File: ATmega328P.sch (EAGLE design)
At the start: 6 parts, among them IC1 MEGA8-P, Q1 16MHz

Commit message: Controller board layout and schematic
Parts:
- added JP1: (no value), pinhead:PINHD-1X3/90
- added JP2, JP3: (no value), pinhead:PINHD-1X5/90
- added JP4: (no value), pinhead:PINHD-1X8/90
- added JP5: (no value), pinhead:PINHD-1X4/90
- added JP6: (no value), pinhead:PINHD-2X3
- added JP7: (no value), pinhead:PINHD-1X3
- R1: value (none) -> 10k
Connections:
- removed net VCC: C3.1, IC1.AREF, IC1.AVCC, IC1.VCC@1, R1.2
- new net 3V3: JP1.3, JP7.3
- new net 5V: C3.1, IC1.AREF, IC1.AVCC, IC1.VCC@1, JP1.1, JP4.1, JP6.2, JP7.1, R1.2
- new net A1: IC1.PC0(ADC0), JP2.1
- new net A2: IC1.PC1(ADC1), JP2.2
- new net B1: IC1.PC2(ADC2), JP2.4
- new net B2: IC1.PC3(ADC3), JP2.5
- new net C1: IC1.PD4(XCK/T0), JP3.1
- new net C2: IC1.PD5(T1), JP3.2
- new net D1: IC1.PD6(AIN0), JP3.4
- new net D2: IC1.PD7(AIN1), JP3.5
- new net INT: IC1.PD2(INT0), JP4.8
- new net N$4: IC1.PB4(MISO), JP6.1
- new net N$7: IC1.PB3(MOSI/OC2), JP6.4
- new net N$8: IC1.PB5(SCK), JP6.3
- new net N$9: IC1.PC6(/RESET), JP6.5, R1.1
- new net RX: IC1.PD0(RXD), JP5.2
- new net SCL: IC1.PC5(ADC5/SCL), JP4.3
- new net SDA: IC1.PC4(ADC4/SDA), JP4.4
- new net TX: IC1.PD1(TXD), JP5.3
- new net XCL: JP4.6
- new net XDA: JP4.5
- net GND: now also JP1.2, JP2.3, JP3.3, JP4.2, JP4.7, JP5.4, JP6.6
- net N$3: now also JP5.1, JP7.2; no longer IC1.PC6(/RESET), R1.1

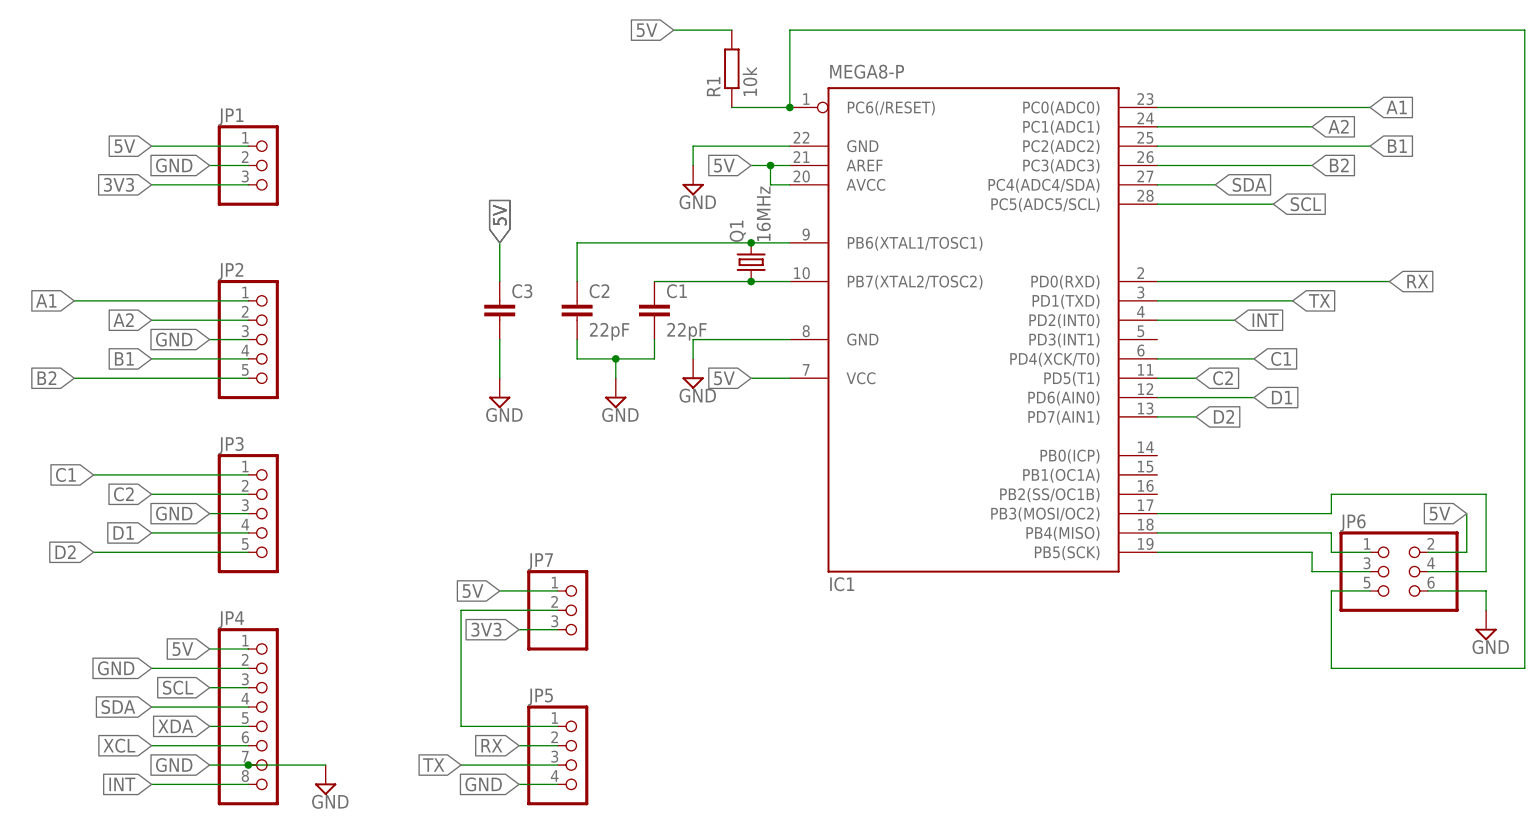
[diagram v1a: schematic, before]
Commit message: Updated layout
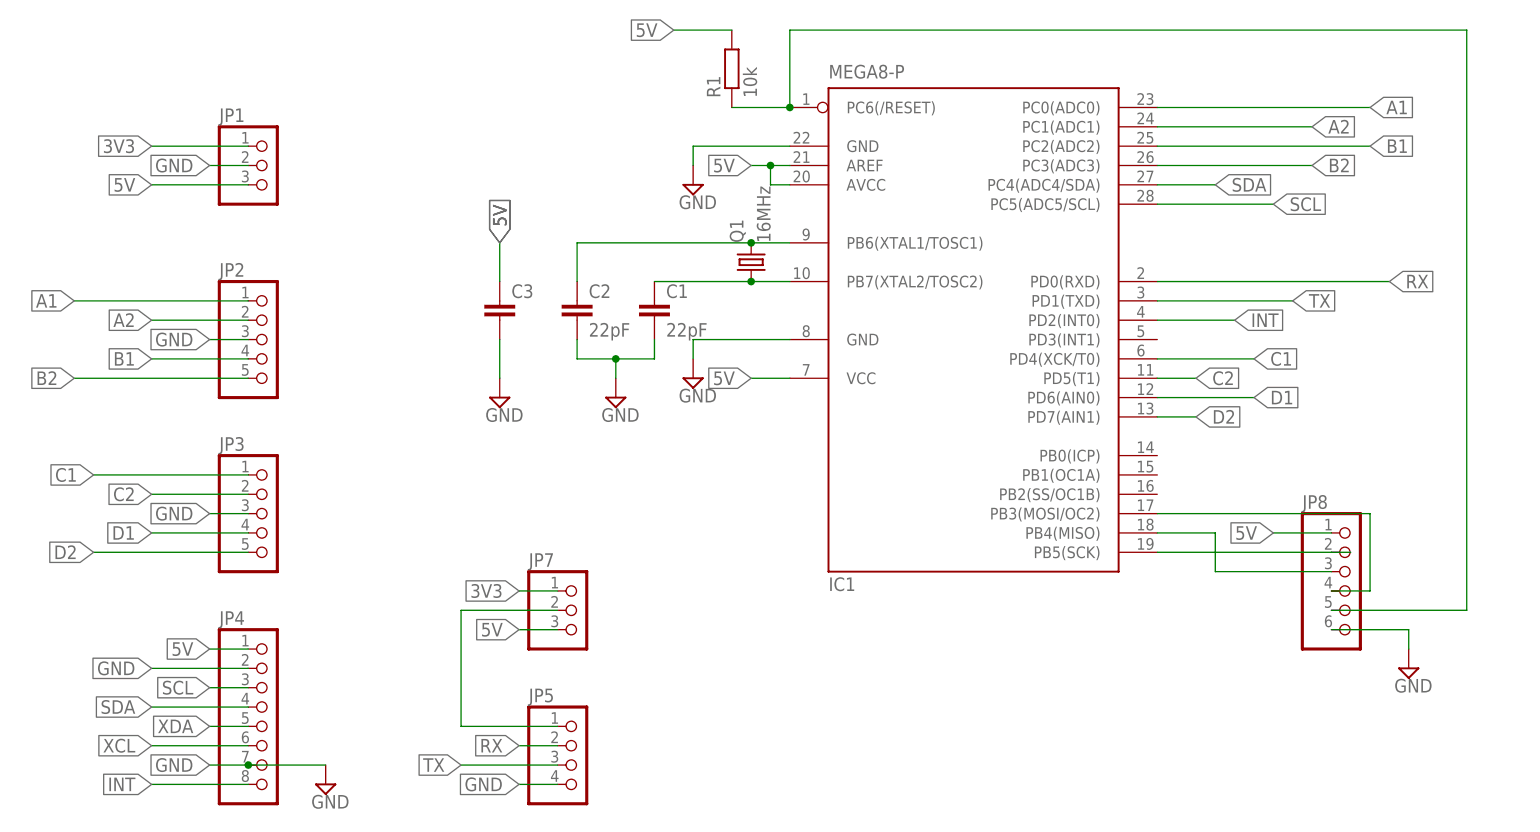
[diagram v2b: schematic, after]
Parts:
- removed JP6: (no value), pinhead:PINHD-2X3
- added JP8: (no value), pinhead:PINHD-1X6
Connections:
- net 3V3: now also JP1.1, JP7.1; no longer JP1.3, JP7.3
- net 5V: now also JP1.3, JP7.3, JP8.1; no longer JP1.1, JP6.2, JP7.1
- net GND: now also JP8.6; no longer JP6.6
- net N$4: now also JP8.3; no longer JP6.1
- net N$7: now also JP8.4; no longer JP6.4
- net N$8: now also JP8.2; no longer JP6.3
- net N$9: now also JP8.5; no longer JP6.5

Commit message: Some adjustments to ISP, pin order matches arduino ISP
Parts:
- JP8: device pinhead:PINHD-1X6 -> pinhead:PINHD-1X5
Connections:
- removed net N$8: IC1.PB5(SCK), JP8.2
- new net N$5: IC1.PB5(SCK), JP8.4
- net 5V: no longer JP8.1
- net GND: now also JP8.5; no longer JP8.6
- net N$7: now also JP8.2; no longer JP8.4
- net N$9: now also JP8.1; no longer JP8.5
